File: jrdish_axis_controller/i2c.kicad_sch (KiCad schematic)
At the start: 16 parts, among them U2 ISO1540QDRQ1, U8 LTC4311ISC6#TRPBF, U9 LM75BIMX-5/NOPB

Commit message: Updates
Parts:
- removed C12, C13: 100nF, PCM_JLCPCB:C_0402, symbol PCM_JLCPCB-Capacitors:0402,100nF
- removed R5, R6: 10kΩ, PCM_JLCPCB:R_0402, symbol PCM_JLCPCB-Resistors:0402,10kΩ
- removed U2: ISO1540QDRQ1, MyParts:SOIC-8_L4.9-W3.9-P1.27-LS6.0-BL, symbol MyParts:ISO1540QDRQ1
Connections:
- net 3.3V_MCU is gone; now on an unnamed net: R2.2
- net GND_MCU is gone; now on net GND: C15.2, C16.2, U9.4 (GND), U9.5 (A2), U9.6 (A1)
- net SDA is gone; now on net SDA_MCU: U8.6 (BUS1)
- net SCL_MCU: now also H2.2, U8.4 (BUS2), U9.2 (SCL)
- net SDA_MCU: now also H1.1, U9.1 (SDA); no longer R2.1
- net at R4.2: now also H2.1; no longer H2.2
- net 3.3V+MCU renamed 3.3V
- net 3.3V: now also C14.1, C17.1, R2.1, R4.1, U8.1 (VCC), U8.3 (ENABLE)
- removed net 5V: C14.1, C17.1, H1.1, H2.1, U8.1 (VCC), U8.3 (ENABLE)
- net GNDIO renamed GND
- removed net SCL: R4.1, U8.4 (BUS2)
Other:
- note added: "H1 and H2 - Optional 10K pull-ups for i2c. 2.54mm jumper."
- note added: "Place the caps close to +VS"
- note added: "The I2C extender has optional pullups. Pullups may not be needed if extended sensors have them."
- note removed: "2 Pin headers for pullup resistors"
- note removed: "IO side"
- note removed: "MCU Side"
- note removed: "No need for pull ups here. The pull ups are already at the I2C isolator. This extender should allow multiple I2C sensors on long wires."
- note removed: "PI I2C Isolator"
- note removed: "Place the 100nF cap close to +VS"
- note removed: "Place the 100nF caps close to VCC1 and VCC2"
- note removed: "This I2C isolator provides capacitive isolation, not opto. Should be good enough for our purposes."
- note removed: "This is after the I2C isolator which has pull-up resistors on the SDA/SCL lines"
- moved on the sheet: C14, C15, C16, C17, U8

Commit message: Passes ERC
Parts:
- added C42: 100nF, PCM_JLCPCB:C_0402, symbol PCM_JLCPCB-Capacitors:0402,100nF,(2)
- added U7: M24C64-RMN6TP, MyParts:SOIC-8_L5.0-W4.0-P1.27-LS6.0-BL, symbol MyParts:M24C64-RMN6TP
- renumbered C17 to C38, C14 to C39, C15 to C40, C16 to C41, H1 to H2, H2 to H3, R2 to R22, R3 to R23, R4 to R24, U8 to U5, U9 to U6
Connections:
- net 3.3V: now also C42.1, U7.8 (VCC)
- net GND: now also C42.2, U7.1 (A0), U7.2 (A1), U7.3 (A2), U7.4 (VSS), U7.7 (#WC)
- net SCL_MCU: now also U7.5 (SDA)
- net SDA_MCU: now also U7.6 (SCL)
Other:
- note added: "8KB, Address will be 0x50"
- note added: "EEPROM"
- moved on the sheet: C38, C39, C40, C41, H2, H3, R22, R23, R24, U5, U6

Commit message: PCB layout in progress
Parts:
- removed C41: 10uF, PCM_JLCPCB:C_0402, symbol PCM_JLCPCB-Capacitors:0402,10uF
- removed C42: 100nF, PCM_JLCPCB:C_0402, symbol PCM_JLCPCB-Capacitors:0402,100nF,(2)
- added C42: 10uF, PCM_JLCPCB:C_0603, symbol PCM_JLCPCB-Capacitors:0603,10uF
- added C43: 100nF, PCM_JLCPCB:C_0402, symbol PCM_JLCPCB-Capacitors:0402,100nF
- added CN7, CN8: SM04B-SRSS-TB (LF)(SN), MyParts:CONN-SMD_4P-P1.00_SM04B-SRSS-TB-LF-SN, symbol MyParts:SM04B-SRSS-TB(LF)(SN)
- renumbered C38 to C39, C39 to C40, C40 to C41, H2 to H3, H3 to H4, R22 to R23, R23 to R24, R24 to R25, U5 to U4, U6 to U5, U7 to U6
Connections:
- net 3.3V: now also C42.1, C43.1, CN7.2, CN8.2
- net GND: now also C42.2, C43.2, CN7.1, CN7.5, CN7.6, CN8.1, CN8.5, CN8.6
- net SCL_MCU: now also CN7.4, CN8.4
- net SDA_MCU: now also CN7.3, CN8.3
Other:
- note added: "I2C Off-board Connectors"
- note added: "Off Board sensors I2C to/from MCU"
- company: (none) -> JRSeti

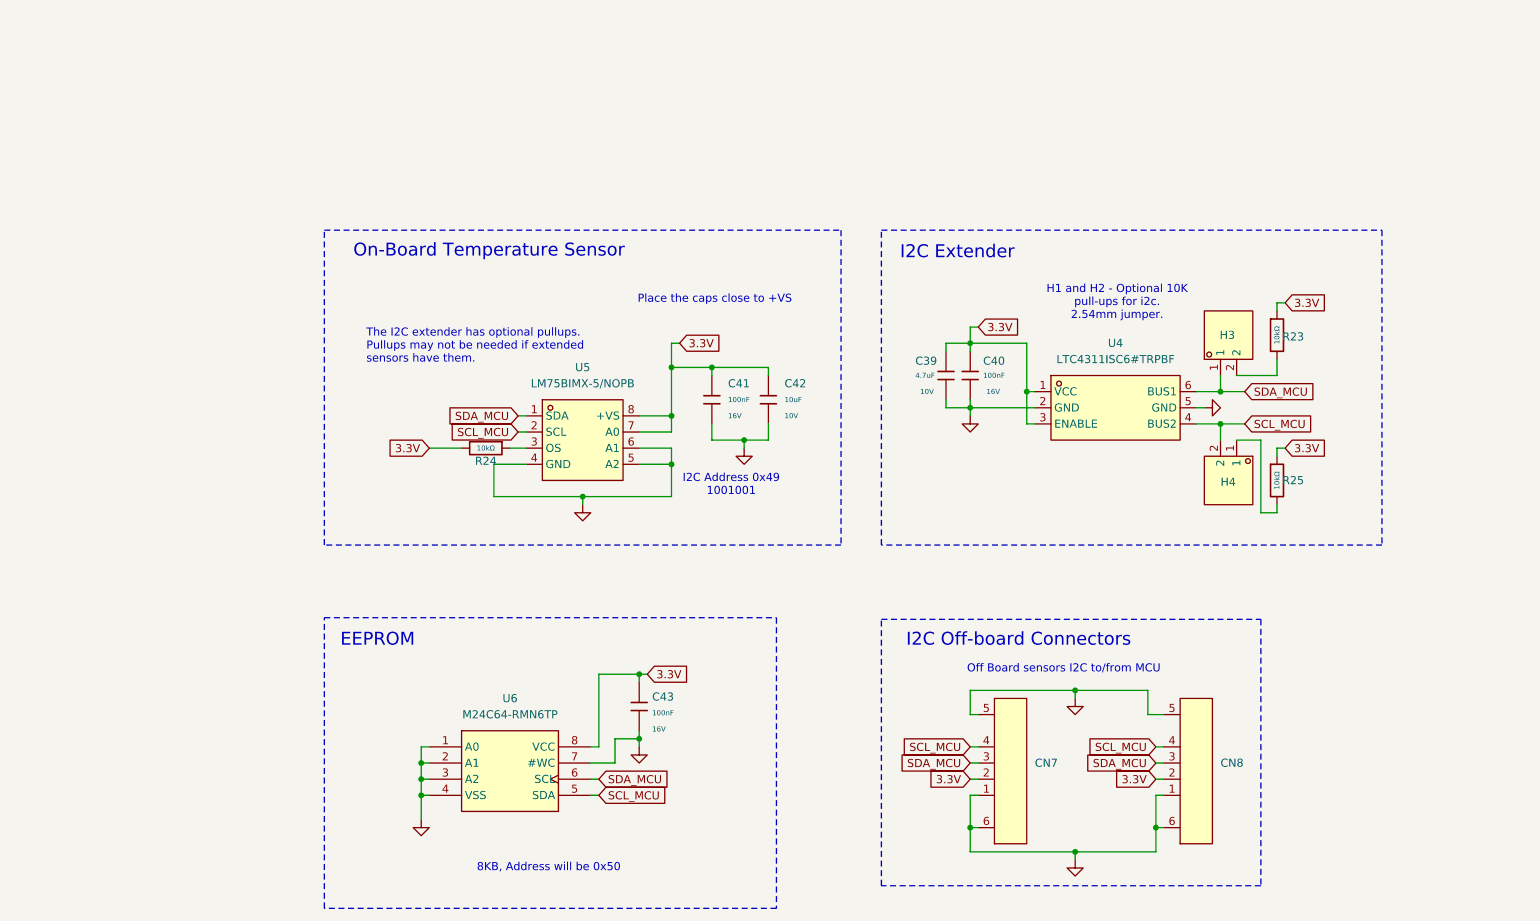
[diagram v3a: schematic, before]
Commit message: New 64pin version - 2 axes
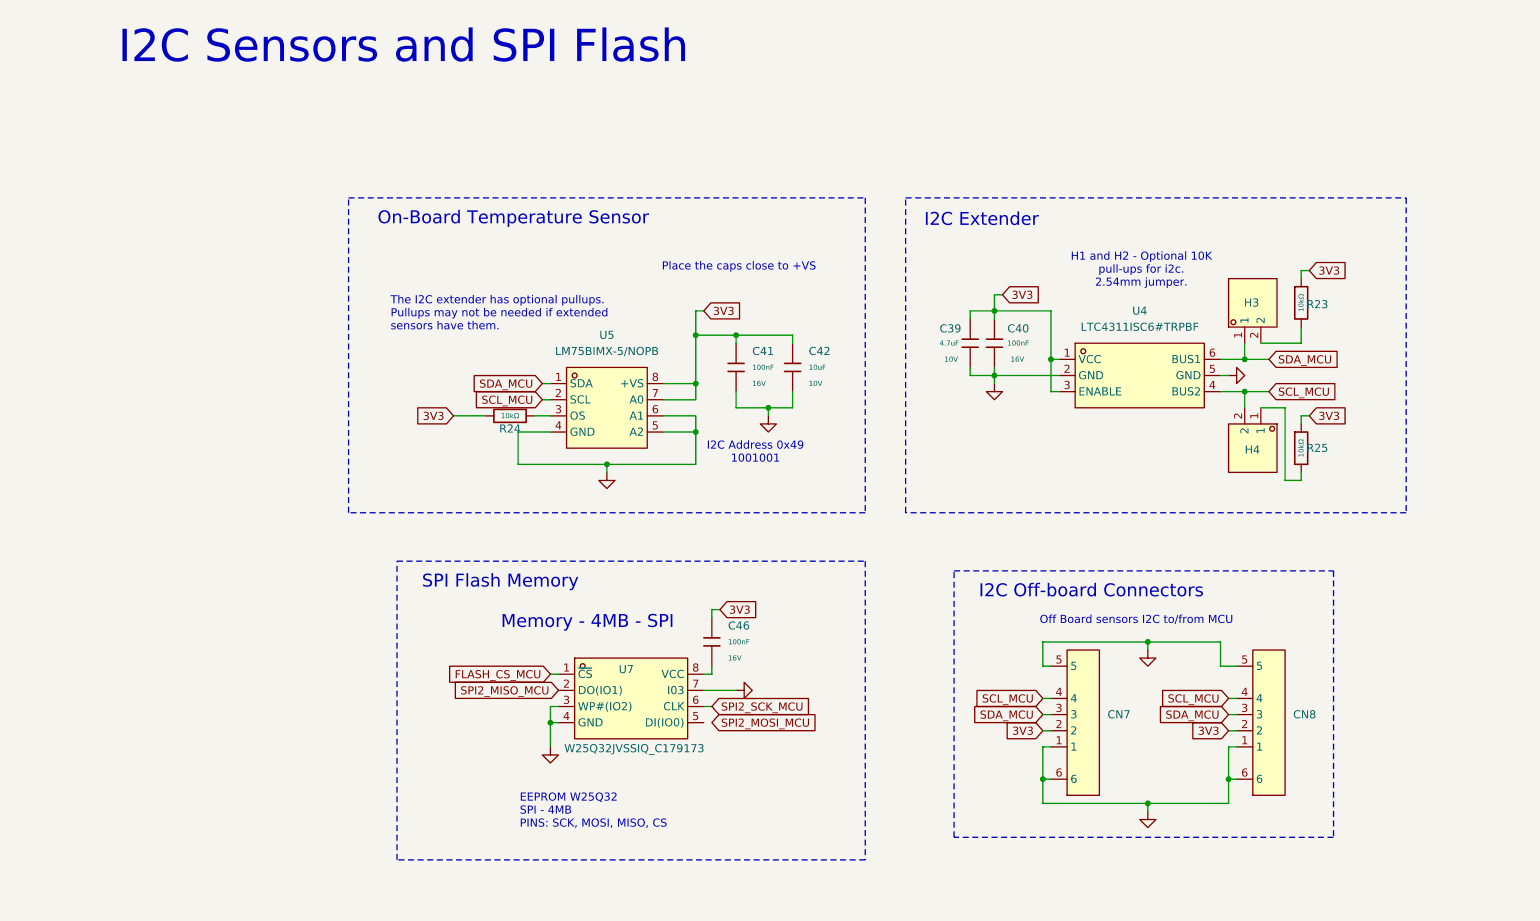
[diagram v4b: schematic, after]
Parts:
- removed C43: 100nF, PCM_JLCPCB:C_0402, symbol PCM_JLCPCB-Capacitors:0402,100nF
- removed U6: M24C64-RMN6TP, MyParts:SOIC-8_L5.0-W4.0-P1.27-LS6.0-BL, symbol MyParts:M24C64-RMN6TP
- added C46: 100nF, PCM_JLCPCB:C_0402, symbol PCM_JLCPCB-Capacitors:0402,100nF
- added U7: W25Q32JVSSIQ_C179173, MyParts:SOIC-8_L5.3-W5.3-P1.27-LS8.0-BL, symbol MyParts:W25Q32JVSSIQ_C179173
- U5: MPN (none) -> LM75BIMX-5/NOPB; Manufacturer (none) -> TI(德州仪器)
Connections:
- net GND: now also U7.3 (WP#(IO2)), U7.4 (GND), U7.7 (I03)
- net 3.3V renamed 3V3
- net 3V3: now also C46.1
- new net: C46.2, U7.8 (VCC)
- new net FLASH_CS_MCU: U7.1 (~{CS})
- new net SPI2_MISO_MCU: U7.2 (DO(IO1))
- new net SPI2_SCK_MCU: U7.6 (CLK)
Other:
- note added: "EEPROM W25Q32 SPI - 4MB PINS: SCK, MOSI, MISO, CS"
- note added: "I2C Sensors and SPI Flash"
- note added: "Memory - 4MB - SPI"
- note added: "SPI Flash Memory"
- note removed: "8KB, Address will be 0x50"
- note removed: "EEPROM"
- moved on the sheet: C39, C40, C41, C42, H3, H4, R23, R24, R25, U4, U5

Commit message: Continuing layout
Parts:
- renumbered C39 to C50, C40 to C51, C41 to C52, C42 to C53, C46 to C54, CN8 to CN7, CN7 to CN8, R23 to R24, R24 to R25, R25 to R26, U4 to U5, U5 to U6
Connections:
- net SPI2_MOSI_MCU: now also U7.5 (DI(IO0))
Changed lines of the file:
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@@
 	(wire
 		(pts
+			(xy 118.11 128.27) (xy 119.38 128.27)
+		)
+		(stroke
+			(width 0)
+			(type default)
+		)
+	)
+	(wire
+		(pts
 			(xy 111.76 82.55) (xy 116.84 82.55)
 		)
@@
 		(in_pos_files yes)
 		(dnp no)
-		(property "Reference" "#PWR043"
+		(property "Reference" "#PWR044"
 			(at 93.98 138.43 0)
 			(hide yes)
@@
 			(project "jrdish_axis_controller"
 				(path "/10d7c3e5-be4d-4306-a59e-500b86bd141f/01e0c1dd-bd55-437a-a4ac-56ab5262d0d8"
-					(reference "#PWR043")
+					(reference "#PWR044")
 					(unit 1)
 				)
@@
 		(dnp no)
 		(fields_autoplaced yes)
-		(property "Reference" "U5"
+		(property "Reference" "U6"
 			(at 102.87 67.31 0)
 			(show_name no)
@@
 			(project "jrdish_axis_controller"
 				(path "/10d7c3e5-be4d-4306-a59e-500b86bd141f/01e0c1dd-bd55-437a-a4ac-56ab5262d0d8"
-					(reference "U5")
+					(reference "U6")
 					(unit 1)
 				)
@@
 		(dnp no)
 		(fields_autoplaced yes)
-		(property "Reference" "U4"
+		(property "Reference" "U5"
 			(at 186.69 63.5 0)
 			(show_name no)
@@
 			(project "jrdish_axis_controller"
 				(path "/10d7c3e5-be4d-4306-a59e-500b86bd141f/01e0c1dd-bd55-437a-a4ac-56ab5262d0d8"
-					(reference "U4")
+					(reference "U5")
 					(unit 1)
 				)
@@
 		(in_pos_files yes)
 		(dnp no)
-		(property "Reference" "C39"
+		(property "Reference" "C50"
 			(at 155.194 66.294 0)
 			(show_name no)
@@
 			(project "jrdish_axis_controller"
 				(path "/10d7c3e5-be4d-4306-a59e-500b86bd141f/01e0c1dd-bd55-437a-a4ac-56ab5262d0d8"
-					(reference "C39")
+					(reference "C50")
 					(unit 1)
 				)
@@
 		(in_pos_files yes)
 		(dnp no)
-		(property "Reference" "C41"
+		(property "Reference" "C52"
 			(at 125.73 69.8499 0)
 			(show_name no)
@@
 			(project "jrdish_axis_controller"
 				(path "/10d7c3e5-be4d-4306-a59e-500b86bd141f/01e0c1dd-bd55-437a-a4ac-56ab5262d0d8"
-					(reference "C41")
+					(reference "C52")
 					(unit 1)
 				)
@@
 		(dnp no)
 		(fields_autoplaced yes)
-		(property "Reference" "#PWR036"
+		(property "Reference" "#PWR040"
 			(at 128.27 86.36 0)
 			(hide yes)
@@
 			(project "jrdish_axis_controller"
 				(path "/10d7c3e5-be4d-4306-a59e-500b86bd141f/01e0c1dd-bd55-437a-a4ac-56ab5262d0d8"
-					(reference "#PWR036")
+					(reference "#PWR040")
 					(unit 1)
 				)
@@
 		(in_pos_files yes)
 		(dnp no)
-		(property "Reference" "#PWR034"
+		(property "Reference" "#PWR038"
 			(at 207.01 73.66 0)
 			(hide yes)
@@
 			(project "jrdish_axis_controller"
 				(path "/10d7c3e5-be4d-4306-a59e-500b86bd141f/01e0c1dd-bd55-437a-a4ac-56ab5262d0d8"
-					(reference "#PWR034")
+					(reference "#PWR038")
 					(unit 1)
 				)
@@
 		(dnp no)
 		(fields_autoplaced yes)
-		(property "Reference" "C46"
+		(property "Reference" "C54"
 			(at 121.92 113.0299 0)
 			(show_name no)
@@
 			(project "jrdish_axis_controller"
 				(path "/10d7c3e5-be4d-4306-a59e-500b86bd141f/01e0c1dd-bd55-437a-a4ac-56ab5262d0d8"
-					(reference "C46")
+					(reference "C54")
 					(unit 1)
 				)
@@
 		(dnp no)
 		(fields_autoplaced yes)
-		(property "Reference" "C42"
+		(property "Reference" "C53"
 			(at 134.62 69.8499 0)
 			(show_name no)
@@
 			(project "jrdish_axis_controller"
 				(path "/10d7c3e5-be4d-4306-a59e-500b86bd141f/01e0c1dd-bd55-437a-a4ac-56ab5262d0d8"
-					(reference "C42")
+					(reference "C53")
 					(unit 1)
 				)
@@
 		(in_pos_files yes)
 		(dnp no)
-		(property "Reference" "CN7"
+		(property "Reference" "CN8"
 			(at 181.61 126.9999 90)
 			(show_name no)
@@
 			(project "jrdish_axis_controller"
 				(path "/10d7c3e5-be4d-4306-a59e-500b86bd141f/01e0c1dd-bd55-437a-a4ac-56ab5262d0d8"
-					(reference "CN7")
+					(reference "CN8")
 					(unit 1)
 				)
@@
 		(in_pos_files yes)
 		(dnp no)
-		(property "Reference" "R24"
+		(property "Reference" "R25"
 			(at 87.63 82.042 90)
 			(show_name no)
@@
 			(project "jrdish_axis_controller"
 				(path "/10d7c3e5-be4d-4306-a59e-500b86bd141f/01e0c1dd-bd55-437a-a4ac-56ab5262d0d8"
-					(reference "R24")
+					(reference "R25")
 					(unit 1)
 				)
@@
 		(in_pos_files yes)
 		(dnp no)
-		(property "Reference" "#PWR044"
+		(property "Reference" "#PWR043"
 			(at 129.54 123.19 0)
 			(hide yes)
@@
 			(project "jrdish_axis_controller"
 				(path "/10d7c3e5-be4d-4306-a59e-500b86bd141f/01e0c1dd-bd55-437a-a4ac-56ab5262d0d8"
-					(reference "#PWR044")
+					(reference "#PWR043")
 					(unit 1)
 				)
@@
 		(dnp no)
 		(fields_autoplaced yes)
-		(property "Reference" "#PWR037"
+		(property "Reference" "#PWR041"
 			(at 102.87 95.25 0)
 			(hide yes)
@@
 			(project "jrdish_axis_controller"
 				(path "/10d7c3e5-be4d-4306-a59e-500b86bd141f/01e0c1dd-bd55-437a-a4ac-56ab5262d0d8"
-					(reference "#PWR037")
+					(reference "#PWR041")
 					(unit 1)
 				)
@@
 		(in_pos_files yes)
 		(dnp no)
-		(property "Reference" "#PWR035"
+		(property "Reference" "#PWR039"
 			(at 163.83 81.28 0)
 			(hide yes)
@@
 			(project "jrdish_axis_controller"
 				(path "/10d7c3e5-be4d-4306-a59e-500b86bd141f/01e0c1dd-bd55-437a-a4ac-56ab5262d0d8"
-					(reference "#PWR035")
+					(reference "#PWR039")
 					(unit 1)
 				)
@@
 		(in_pos_files yes)
 		(dnp no)
-		(property "Reference" "R25"
+		(property "Reference" "R26"
 			(at 214.63 85.09 0)
 			(show_name no)
@@
 			(project "jrdish_axis_controller"
 				(path "/10d7c3e5-be4d-4306-a59e-500b86bd141f/01e0c1dd-bd55-437a-a4ac-56ab5262d0d8"
-					(reference "R25")
+					(reference "R26")
 					(unit 1)
 				)
@@
 		(in_pos_files yes)
 		(dnp no)
-		(property "Reference" "CN8"
+		(property "Reference" "CN7"
 			(at 210.82 126.9999 90)
 			(show_name no)
@@
 			(project "jrdish_axis_controller"
 				(path "/10d7c3e5-be4d-4306-a59e-500b86bd141f/01e0c1dd-bd55-437a-a4ac-56ab5262d0d8"
-					(reference "CN8")
+					(reference "CN7")
 					(unit 1)
 				)
@@
 		(in_pos_files yes)
 		(dnp no)
-		(property "Reference" "C40"
+		(property "Reference" "C51"
 			(at 165.862 66.294 0)
 			(show_name no)
@@
 			(project "jrdish_axis_controller"
 				(path "/10d7c3e5-be4d-4306-a59e-500b86bd141f/01e0c1dd-bd55-437a-a4ac-56ab5262d0d8"
-					(reference "C40")
+					(reference "C51")
 					(unit 1)
 				)
@@
 		(in_pos_files yes)
 		(dnp no)
-		(property "Reference" "R23"
+		(property "Reference" "R24"
 			(at 214.63 62.484 0)
 			(show_name no)
@@
 			(project "jrdish_axis_controller"
 				(path "/10d7c3e5-be4d-4306-a59e-500b86bd141f/01e0c1dd-bd55-437a-a4ac-56ab5262d0d8"
-					(reference "R23")
+					(reference "R24")
 					(unit 1)
 				)
